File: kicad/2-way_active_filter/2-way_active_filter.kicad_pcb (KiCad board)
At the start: 2 copper layers, 112 x 109.6 mm, 147 parts

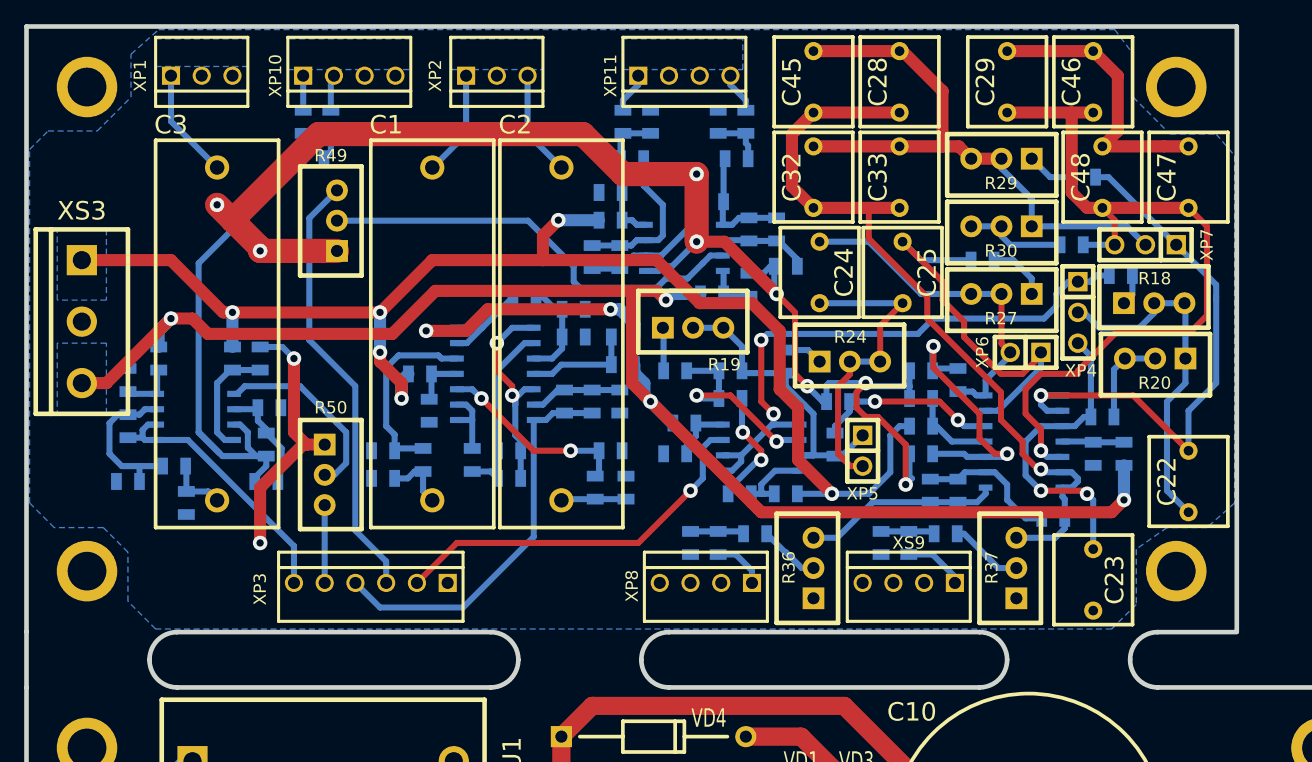
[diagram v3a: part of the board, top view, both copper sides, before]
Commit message: Send to production of 2-way active filter.
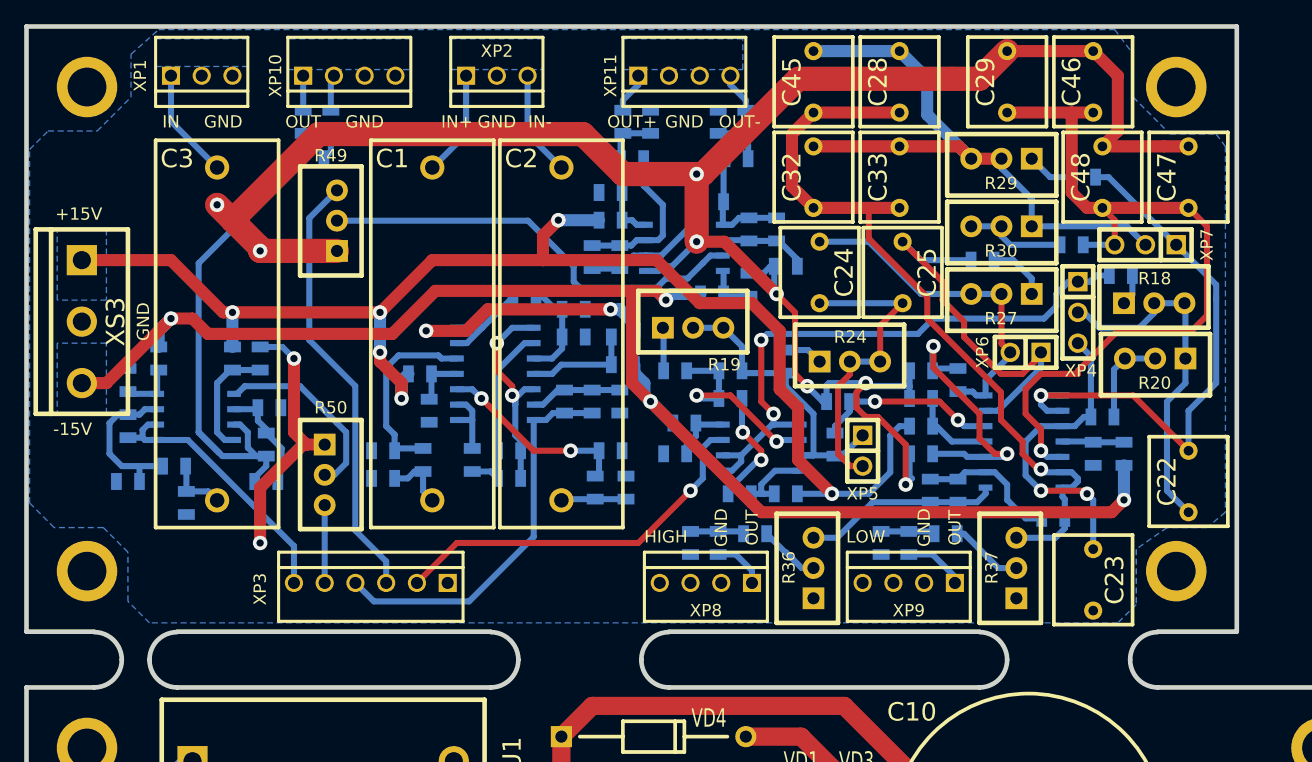
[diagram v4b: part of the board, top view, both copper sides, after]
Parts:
- renumbered XS9 to XP9
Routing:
- net /GND: track 191.5 -> 221.3 mm
- net /CAP1: track 53.9 -> 51.1 mm
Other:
- outline, holes or cut-outs redrawn
- board text added: "+15V"
- board text added: "-15V"
- board text added: "GND"
- board text added: "HIGH"
- board text added: "IN"
- board text added: "IN+"
- board text added: "IN-"
- board text added: "LOW"
- board text added: "OUT"
- board text added: "OUT+"
- board text added: "OUT-"
